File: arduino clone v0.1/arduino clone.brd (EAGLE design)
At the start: 70.3 x 27.6 mm, 47 parts, among them J203 ICSP HEADER, J402 FTDI Breakout Header, U101 ATMEGA328P_TQFP, U301 CH340G, Y101 16MHz, Y301 12MHz

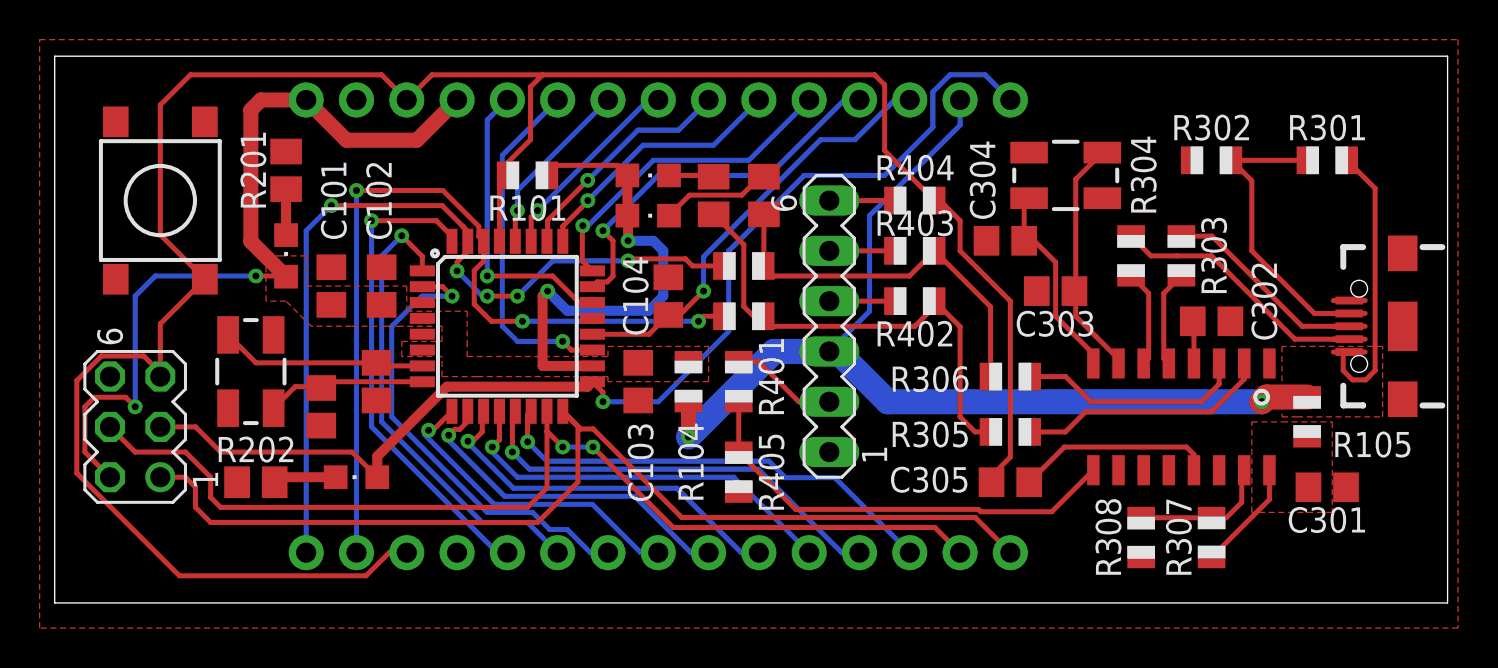
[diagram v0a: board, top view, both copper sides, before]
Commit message: move around traces to shrink board outline
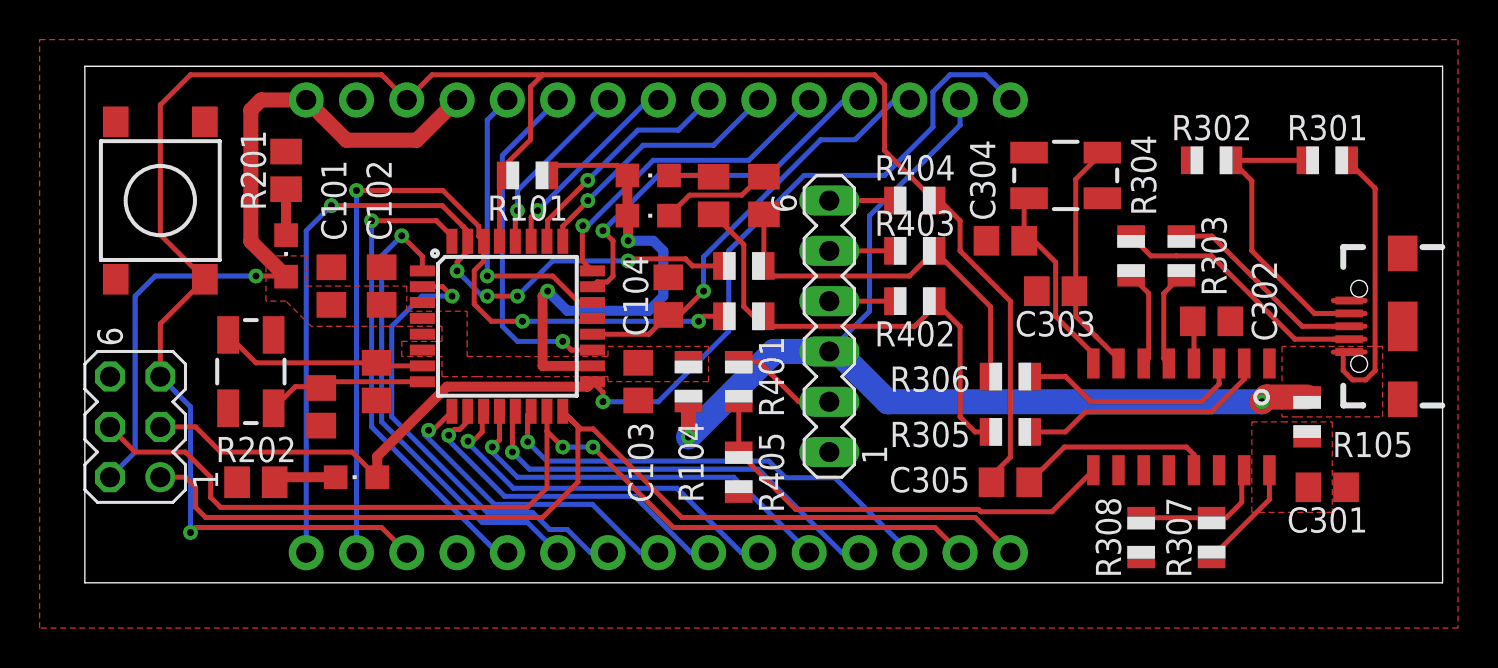
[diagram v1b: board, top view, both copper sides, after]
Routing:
- net MCU_RESET: track 115.9 -> 106.9 mm, vias 0 -> 1
- net PP5V0_MCU: track 67.1 -> 64.1 mm, vias 4 -> 3
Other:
- board size 70.3 x 27.6 mm -> 68.6 x 26.1 mm
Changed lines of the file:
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@@
 <board>
 <plain>
-<wire x1="11.43" y1="38.1" x2="81.768" y2="38.1" width="0" layer="20"/>
-<wire x1="81.768" y1="38.1" x2="81.768" y2="65.71" width="0" layer="20"/>
-<wire x1="81.768" y1="65.71" x2="11.43" y2="65.71" width="0" layer="20"/>
-<wire x1="11.43" y1="65.71" x2="11.43" y2="38.1" width="0" layer="20"/>
+<wire x1="12.954" y1="39.116" x2="81.514" y2="39.116" width="0" layer="20"/>
+<wire x1="81.514" y1="39.116" x2="81.514" y2="65.202" width="0" layer="20"/>
+<wire x1="81.514" y1="65.202" x2="12.954" y2="65.202" width="0" layer="20"/>
+<wire x1="12.954" y1="65.202" x2="12.954" y2="39.116" width="0" layer="20"/>
 </plain>
 <attributes>
@@
 </polygon>
 <contactref element="J203" pad="2"/>
-<wire x1="14.224" y1="44.45" x2="12.954" y2="45.72" width="0.254" layer="1"/>
-<wire x1="12.954" y1="45.72" x2="12.954" y2="48.006" width="0.254" layer="1"/>
-<wire x1="12.954" y1="48.006" x2="13.4366" y2="48.4886" width="0.254" layer="1"/>
 <wire x1="23.114" y1="54.576" x2="23.08" y2="54.61" width="0.254" layer="1"/>
 <wire x1="23.08" y1="54.61" x2="21.59" y2="54.61" width="0.254" layer="1"/>
 <via x="21.59" y="54.61" extent="1-16" drill="0.35"/>
-<wire x1="13.4366" y1="48.4886" x2="15.0114" y2="48.4886" width="0.254" layer="1"/>
-<wire x1="15.494" y1="48.006" x2="15.0114" y2="48.4886" width="0.254" layer="1"/>
-<via x="15.494" y="48.006" extent="1-16" drill="0.35"/>
-<wire x1="15.494" y1="48.006" x2="15.494" y2="53.594" width="0.254" layer="16"/>
-<wire x1="15.494" y1="53.594" x2="16.51" y2="54.61" width="0.254" layer="16"/>
+<wire x1="16.51" y1="54.61" x2="15.494" y2="53.594" width="0.254" layer="16"/>
 <wire x1="16.51" y1="54.61" x2="21.59" y2="54.61" width="0.254" layer="16"/>
 <wire x1="40.352" y1="59.69" x2="40.352" y2="57.658" width="0.508" layer="1"/>
@@
 <wire x1="21.336" y1="62.992" x2="21.336" y2="56.354" width="0.762" layer="1"/>
 <wire x1="21.336" y1="56.354" x2="23.08" y2="54.61" width="0.762" layer="1"/>
+<wire x1="15.494" y1="45.72" x2="14.224" y2="44.45" width="0.254" layer="16"/>
+<wire x1="15.494" y1="53.594" x2="15.494" y2="45.72" width="0.254" layer="16"/>
 </signal>
 <signal name="GND">
@@
 <wire x1="27.94" y1="64.77" x2="18.288" y2="64.77" width="0.254" layer="1"/>
 <wire x1="16.764" y1="56.695" x2="16.764" y2="63.246" width="0.254" layer="1"/>
-<wire x1="13.7926375" y1="50.5714" x2="15.9253625" y2="50.5714" width="0.254" layer="1"/>
-<wire x1="29.21" y1="40.64" x2="28.32236875" y2="40.64" width="0.254" layer="1"/>
-<wire x1="28.32236875" y1="40.64" x2="27.15396875" y2="39.4716" width="0.254" layer="1"/>
-<wire x1="12.5476" y1="44.6536375" x2="12.5476" y2="49.3263625" width="0.254" layer="1"/>
-<wire x1="12.5476" y1="49.3263625" x2="13.7926375" y2="50.5714" width="0.254" layer="1"/>
-<wire x1="27.15396875" y1="39.4716" x2="17.7296375" y2="39.4716" width="0.254" layer="1"/>
-<wire x1="17.7296375" y1="39.4716" x2="12.5476" y2="44.6536375" width="0.254" layer="1"/>
-<wire x1="15.9253625" y1="50.5714" x2="16.764" y2="49.7327625" width="0.254" layer="1"/>
 <wire x1="16.764" y1="49.7327625" x2="16.764" y2="49.53" width="0.254" layer="1"/>
 <wire x1="19.014" y1="54.445" x2="16.764" y2="56.695" width="0.254" layer="1"/>
@@
 <wire x1="30.48" y1="64.77" x2="36.068" y2="64.77" width="0.254" layer="1"/>
 <wire x1="29.21" y1="63.5" x2="27.94" y2="64.77" width="0.254" layer="1"/>
+<wire x1="27.94" y1="41.91" x2="29.21" y2="40.64" width="0.254" layer="1"/>
+<wire x1="16.764" y1="49.53" x2="18.288" y2="48.006" width="0.254" layer="16"/>
+<wire x1="18.288" y1="48.006" x2="18.288" y2="41.656" width="0.254" layer="16"/>
+<via x="18.288" y="41.656" extent="1-16" drill="0.35"/>
+<wire x1="18.288" y1="41.656" x2="18.542" y2="41.91" width="0.254" layer="1"/>
+<wire x1="18.542" y1="41.91" x2="27.94" y2="41.91" width="0.254" layer="1"/>
 </signal>
 <signal name="MCU_AREF">
@@
 <wire x1="18.034" y1="44.45" x2="18.542" y2="43.942" width="0.254" layer="1"/>
 <wire x1="18.542" y1="43.942" x2="18.542" y2="42.926" width="0.254" layer="1"/>
-<wire x1="18.542" y1="42.926" x2="19.304" y2="42.164" width="0.254" layer="1"/>
+<wire x1="18.542" y1="42.926" x2="19.05" y2="42.418" width="0.254" layer="1"/>
 <wire x1="37.852" y1="44.202" x2="37.852" y2="47.0154" width="0.254" layer="1"/>
-<wire x1="19.304" y1="42.164" x2="35.814" y2="42.164" width="0.254" layer="1"/>
-<wire x1="35.814" y1="42.164" x2="37.852" y2="44.202" width="0.254" layer="1"/>
+<wire x1="19.05" y1="42.418" x2="36.068" y2="42.418" width="0.254" layer="1"/>
+<wire x1="36.068" y1="42.418" x2="37.852" y2="44.202" width="0.254" layer="1"/>
 <wire x1="37.852" y1="47.0154" x2="37.09" y2="47.7774" width="0.254" layer="1"/>
 <wire x1="59.69" y1="40.64" x2="57.912" y2="42.418" width="0.254" layer="1"/>

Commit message: round corners
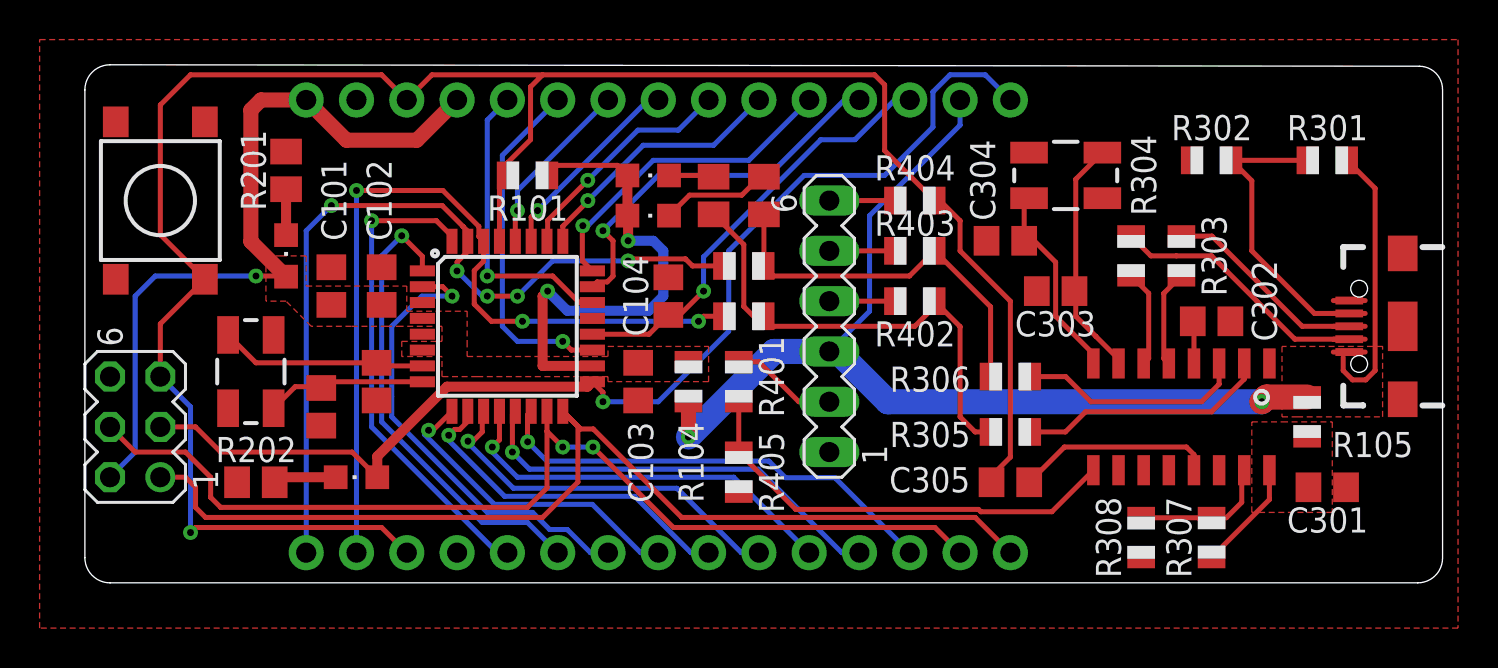
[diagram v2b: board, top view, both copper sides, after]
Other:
- board size 68.6 x 26.1 mm -> 68.6 x 26.2 mm
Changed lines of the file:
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@@
 <setting verticaltext="up"/>
 </settings>
-<grid distance="10" unitdist="mil" unit="mil" style="lines" multiple="1" display="yes" altdistance="5" altunitdist="mil" altunit="mil"/>
+<grid distance="10" unitdist="mil" unit="mil" style="lines" multiple="1" display="yes" altdistance="1" altunitdist="mil" altunit="mil"/>
 <layers>
 <layer number="1" name="Top" color="4" fill="1" visible="yes" active="yes"/>
@@
 <board>
 <plain>
-<wire x1="12.954" y1="39.116" x2="81.514" y2="39.116" width="0" layer="20"/>
-<wire x1="81.514" y1="39.116" x2="81.514" y2="65.202" width="0" layer="20"/>
-<wire x1="81.514" y1="65.202" x2="12.954" y2="65.202" width="0" layer="20"/>
-<wire x1="12.954" y1="65.202" x2="12.954" y2="39.116" width="0" layer="20"/>
+<wire x1="12.954" y1="64.008846875" x2="12.954" y2="40.386" width="0" layer="20"/>
+<wire x1="12.954" y1="40.386" x2="14.224" y2="39.116" width="0" layer="20" curve="90"/>
+<wire x1="14.224" y1="39.116" x2="80.264" y2="39.116" width="0" layer="20"/>
+<wire x1="80.264" y1="39.116" x2="81.514" y2="40.366" width="0" layer="20" curve="90"/>
+<wire x1="81.514" y1="40.366" x2="81.514" y2="64.02745625" width="0" layer="20"/>
+<wire x1="81.514" y1="64.02745625" x2="80.33945625" y2="65.20330625" width="0" layer="20" curve="90"/>
+<wire x1="80.33945625" y1="65.20330625" x2="14.223353125" y2="65.276790625" width="0" layer="20"/>
+<wire x1="14.223353125" y1="65.276790625" x2="12.954" y2="64.008846875" width="0" layer="20" curve="90"/>
 </plain>
 <attributes>

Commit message: add gnd plane on bottom
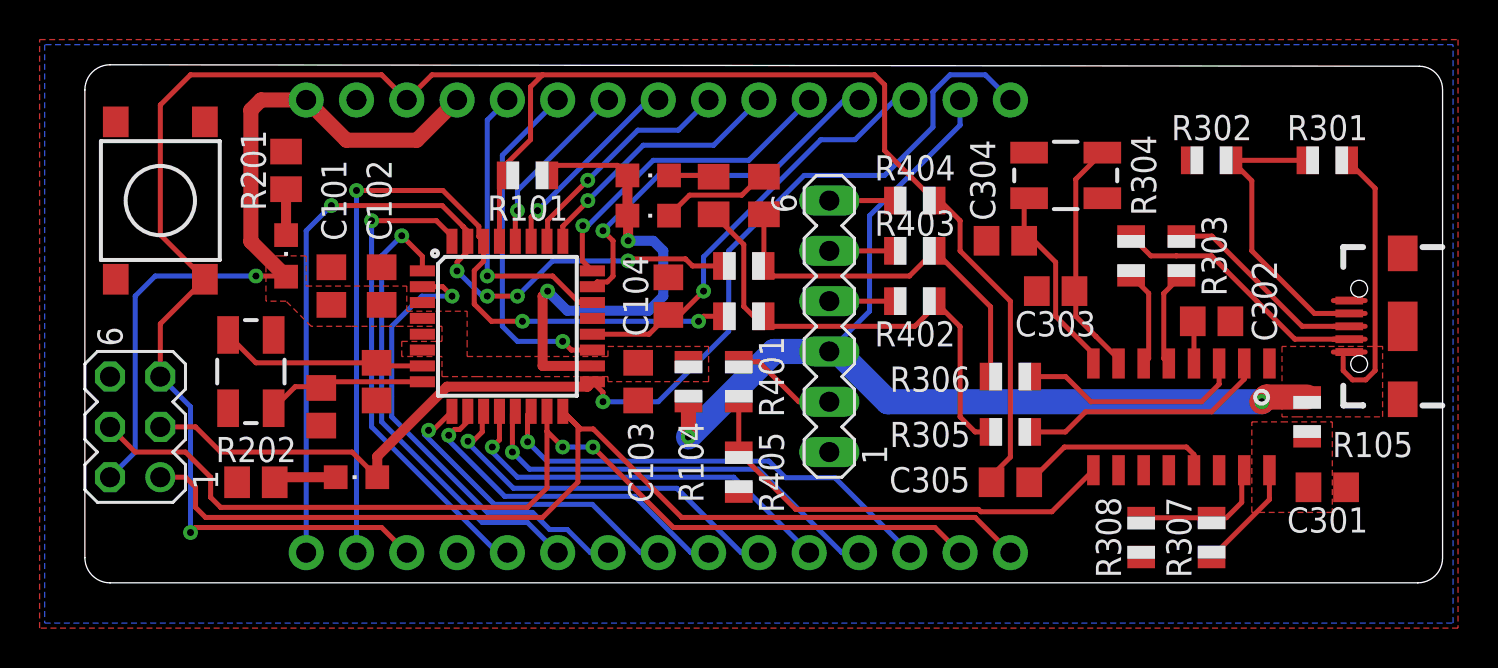
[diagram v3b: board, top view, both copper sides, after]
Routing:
- added copper zone on layer 16, net GND
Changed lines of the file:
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@@
 <vertex x="10.668" y="36.83"/>
 </polygon>
+<polygon width="0.0762" layer="16" rank="6">
+<vertex x="10.922" y="66.294"/>
+<vertex x="10.922" y="37.084"/>
+<vertex x="82.042" y="37.084"/>
+<vertex x="82.042" y="66.294"/>
+</polygon>
+<wire x1="72.771" y1="50.193" x2="76.802" y2="53.37" width="0" layer="19" extent="1-1"/>
+<wire x1="70.8" y1="52.324" x2="72.771" y2="50.193" width="0" layer="19" extent="1-1"/>
+<wire x1="76.642" y1="43.942" x2="72.771" y2="50.193" width="0" layer="19" extent="1-1"/>
+<wire x1="68.85" y1="60.452" x2="70.8" y2="52.324" width="0" layer="19" extent="1-1"/>
+<wire x1="61.026" y1="53.848" x2="70.8" y2="52.324" width="0" layer="19" extent="1-1"/>
+<wire x1="58.486" y1="56.388" x2="61.026" y2="53.848" width="0" layer="19" extent="1-1"/>
+<wire x1="66.294" y1="40.402" x2="76.642" y2="43.942" width="0" layer="19" extent="1-1"/>
+<wire x1="50.546" y1="45.72" x2="61.026" y2="53.848" width="0" layer="19" extent="1-1"/>
+<wire x1="45.974" y1="43.704" x2="50.546" y2="45.72" width="0" layer="19" extent="1-1"/>
+<wire x1="40.894" y1="48.326" x2="45.974" y2="43.704" width="0" layer="19" extent="1-1"/>
+<wire x1="38.5826" y1="52.47" x2="40.894" y2="48.326" width="0" layer="19" extent="1-1"/>
+<wire x1="42.418" y1="54.544" x2="38.5826" y2="52.47" width="0" layer="19" extent="1-1"/>
+<wire x1="29.9974" y1="51.67" x2="38.5826" y2="52.47" width="0" layer="19" extent="1-1"/>
+<wire x1="29.9974" y1="53.27" x2="29.9974" y2="51.67" width="0" layer="19" extent="1-1"/>
+<wire x1="27.94" y1="55.052" x2="29.9974" y2="53.27" width="0" layer="19" extent="1-1"/>
+<wire x1="25.4" y1="55.052" x2="27.94" y2="55.052" width="0" layer="19" extent="1-1"/>
+<wire x1="27.686" y1="48.326" x2="29.9974" y2="51.67" width="0" layer="19" extent="1-1"/>
+<wire x1="24.892" y1="47.056" x2="27.686" y2="48.326" width="0" layer="19" extent="1-1"/>
+<wire x1="20.64" y1="44.196" x2="24.892" y2="47.056" width="0" layer="19" extent="1-1"/>
+<wire x1="23.114" y1="60.894" x2="25.4" y2="55.052" width="0" layer="19" extent="1-1"/>
+<wire x1="26.67" y1="63.5" x2="23.114" y2="60.894" width="0" layer="19" extent="1-1"/>
+<wire x1="14.224" y1="49.53" x2="20.64" y2="44.196" width="0" layer="19" extent="1-1"/>
+<wire x1="14.514" y1="54.445" x2="14.224" y2="49.53" width="0" layer="19" extent="1-1"/>
+<wire x1="31.75" y1="40.64" x2="27.686" y2="48.326" width="0" layer="19" extent="1-1"/>
 </signal>
 <signal name="MCU_RESET">
